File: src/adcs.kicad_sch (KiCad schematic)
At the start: 0 parts

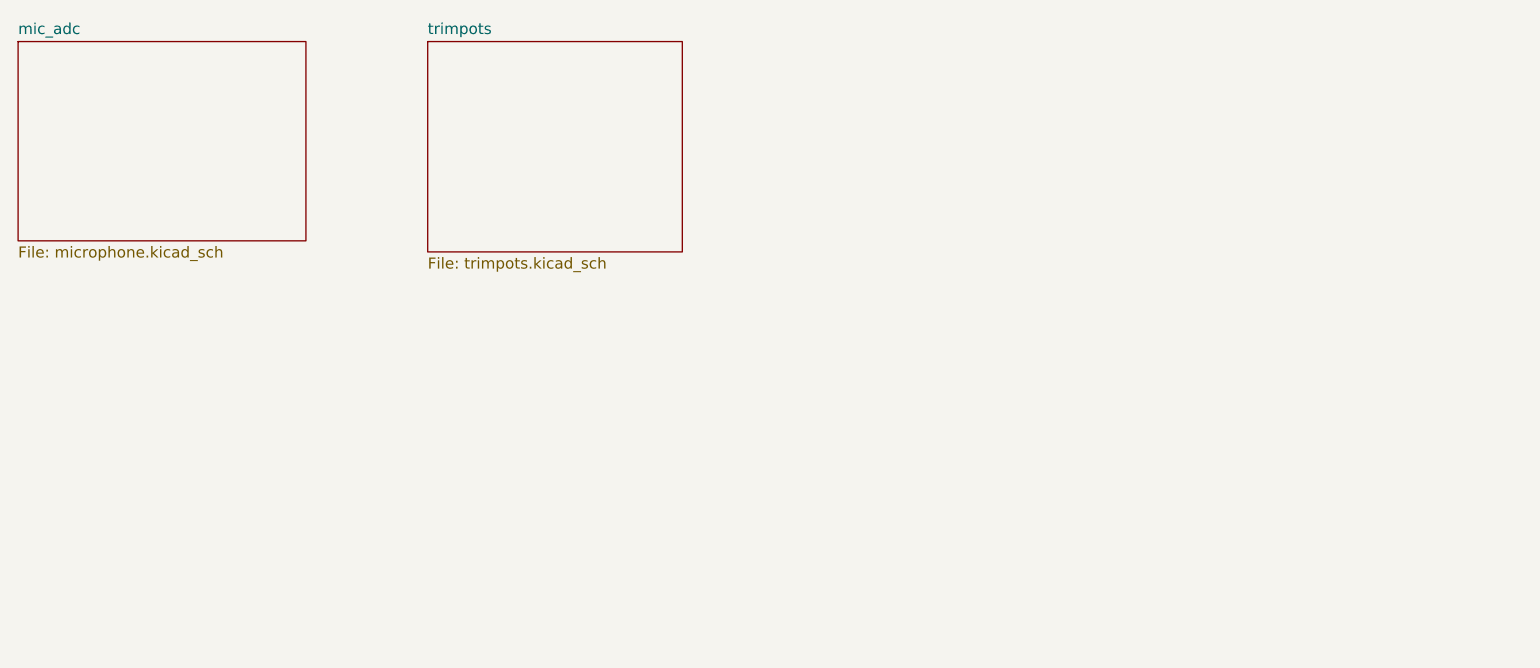
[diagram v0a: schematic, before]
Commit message: fix: Consertando paginação e refact da Tela_OLED
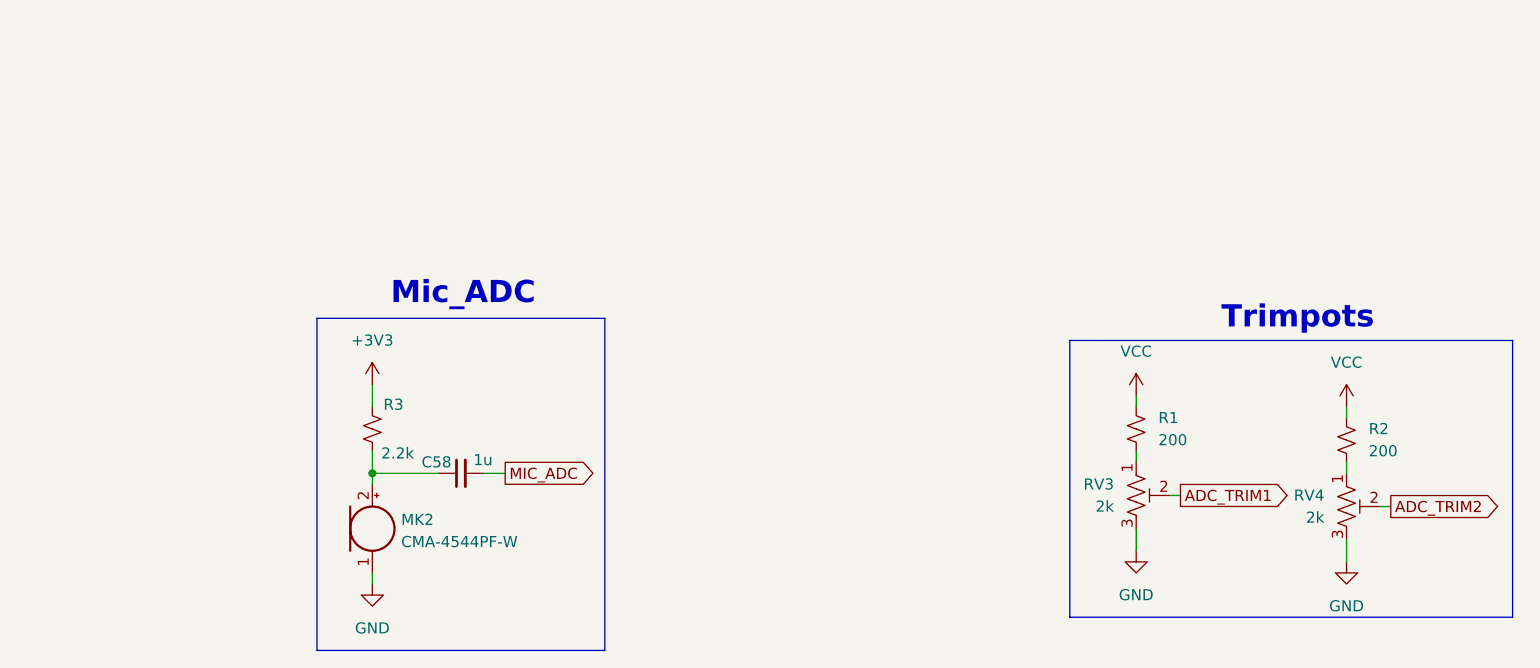
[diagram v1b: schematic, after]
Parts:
- added C58: 1u, Capacitor_SMD:C_0402_1005Metric, symbol Device:C_Small
- added MK2: CMA-4544PF-W, symbol Device:Microphone
- added R1, R2: 200, symbol Device:R_Small_US
- added R3: 2.2k, Resistor_SMD:R_0402_1005Metric, symbol Device:R_Small_US
- added RV3, RV4: 2k, symbol Device:R_Potentiometer_Trim_US
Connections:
- new net: C58.1, MK2.2 (+), R3.2
- new net: R2.2, RV4.1
- new net: R1.2, RV3.1
- new net +3V3: R3.1
- new net ADC_TRIM1: RV3.2
- new net ADC_TRIM2: RV4.2
- new net GND: MK2.1 (-), RV3.3, RV4.3
- new net MIC_ADC: C58.2
- new net VCC: R1.1, R2.1
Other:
- removed sheet mic_adc
- removed sheet trimpots
- note added: "Mic_ADC"
- note added: "Trimpots"

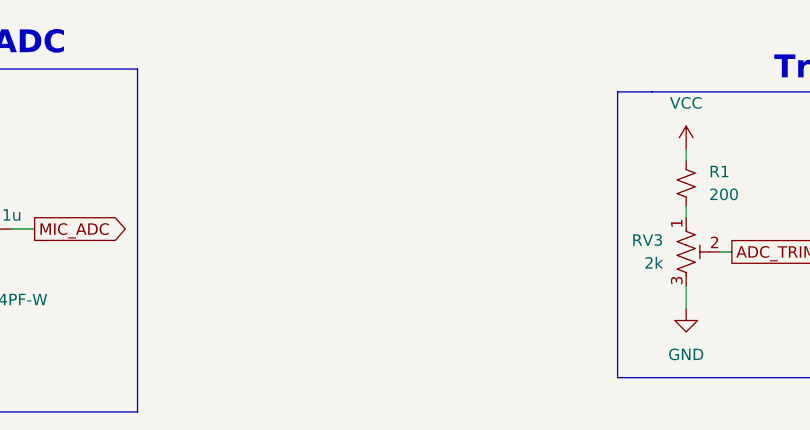
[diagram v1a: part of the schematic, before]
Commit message: LDR adicionado
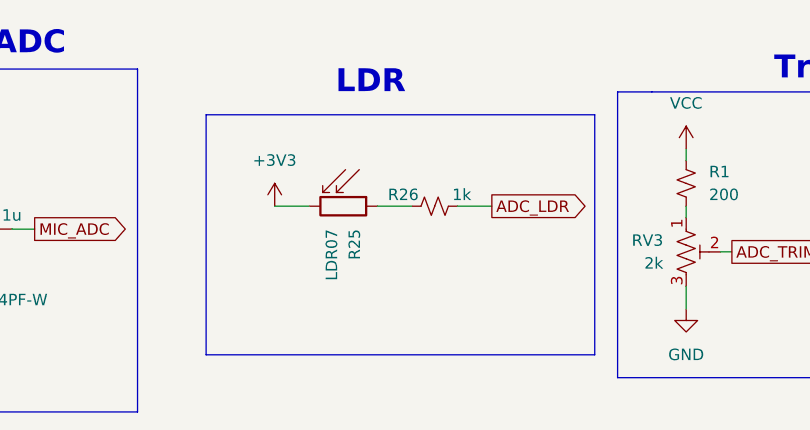
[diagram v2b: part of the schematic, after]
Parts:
- added R25: LDR07, OptoDevice:R_LDR_5.1x4.3mm_P3.4mm_Vertical, symbol Sensor_Optical:LDR07
- added R26: 1k, symbol Device:R_Small_US
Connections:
- net +3V3: now also R25.2
- new net: R25.1, R26.2
- new net ADC_LDR: R26.1
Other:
- note added: "LDR"

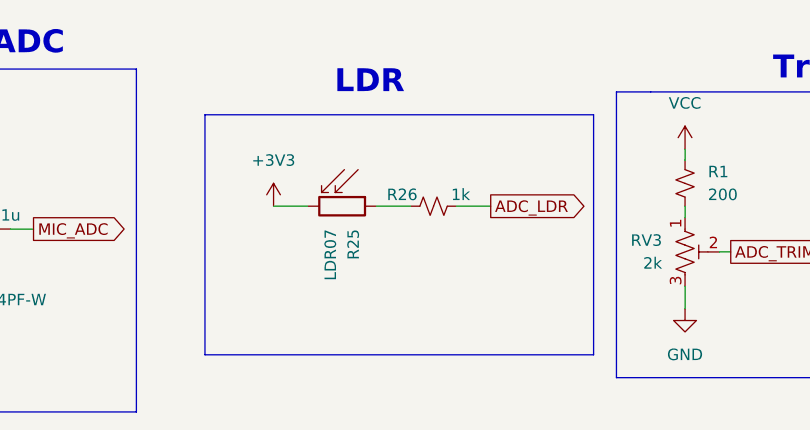
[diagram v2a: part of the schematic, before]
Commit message: adicionado footprints, falta microfone e display somente
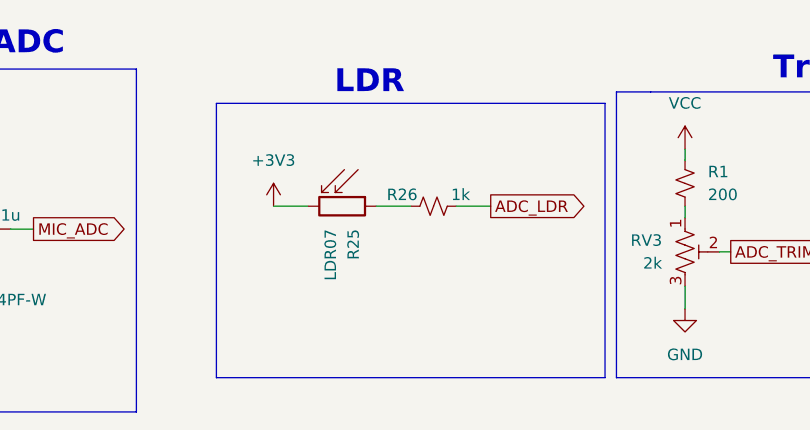
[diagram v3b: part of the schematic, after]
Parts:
- R1, R2, R26: footprint (none) -> Resistor_SMD:R_0402_1005Metric
- RV3, RV4: footprint (none) -> Potentiometer_SMD:Potentiometer_Bourns_TC33X_Vertical
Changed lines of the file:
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@@
-		)
-	)
-	(text_box ""
-		(exclude_from_sim no)
-		(at 116.84 85.09 0)
-		(size 43.18 26.67)
-		(margins 0.9525 0.9525 0.9525 0.9525)
-		(stroke
-			(width 0)
-			(type solid)
-		)
-		(fill
-			(type none)
-		)
-		(effects
-			(font
-				(size 1.27 1.27)
-			)
-			(justify left top)
 		)
 	)
@@
 		(color 0 0 0 0)
 	)
+	(polyline
+		(pts
+			(xy 118.11 83.82) (xy 161.29 83.82)
+		)
+		(stroke
+			(width 0)
+			(type default)
+		)
+	)
 	(wire
 		(pts
@@
 		)
 	)
+	(polyline
+		(pts
+			(xy 161.29 114.3) (xy 161.29 83.82)
+		)
+		(stroke
+			(width 0)
+			(type default)
+		)
+	)
+	(polyline
+		(pts
+			(xy 118.11 114.3) (xy 161.29 114.3)
+		)
+		(stroke
+			(width 0)
+			(type default)
+		)
+	)
 	(wire
 		(pts
@@
 		(pts
 			(xy 170.18 104.14) (xy 170.18 106.68)
+		)
+		(stroke
+			(width 0)
+			(type default)
+		)
+	)
+	(polyline
+		(pts
+			(xy 118.11 83.82) (xy 118.11 114.3)
 		)
 		(stroke
@@
 			)
 		)
-		(property "Footprint" ""
+		(property "Footprint" "Potentiometer_SMD:Potentiometer_Bourns_TC33X_Vertical"
 			(at 194.31 101.6 0)
 			(effects
@@
 			)
 		)
-		(property "Footprint" ""
+		(property "Footprint" "Potentiometer_SMD:Potentiometer_Bourns_TC33X_Vertical"
 			(at 170.18 100.33 0)
 			(effects
@@
 			)
 		)
-		(property "Footprint" ""
+		(property "Footprint" "Resistor_SMD:R_0402_1005Metric"
 			(at 194.31 93.98 0)
 			(effects
@@
 			)
 		)
-		(property "Footprint" ""
+		(property "Footprint" "Resistor_SMD:R_0402_1005Metric"
 			(at 142.24 95.25 0)
 			(effects
@@
 			)
 		)
-		(property "Footprint" ""
+		(property "Footprint" "Resistor_SMD:R_0402_1005Metric"
 			(at 170.18 92.71 0)
 			(effects

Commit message: pequenos ajustes nas tags
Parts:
- MK2: footprint (none) -> componentes_personalizados:MIC_CMA-4544PF-W
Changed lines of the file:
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@@
 			)
 		)
-		(property "Footprint" ""
+		(property "Footprint" "componentes_personalizados:MIC_CMA-4544PF-W"
 			(at 82.55 101.6 90)
 			(effects
